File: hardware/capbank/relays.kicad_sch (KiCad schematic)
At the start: 13 parts, among them K1 3570.1333.121 COMUS, K2 3570.1333.121 COMUS, K4 3570.1333.121 COMUS, U1 ULN2003

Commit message: KiCad changes
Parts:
- added D10, D11, D9: LED, PCM_Diode_SMD_Handsoldering_AKL:D_0603_1608Metric, symbol Device:LED
- added R11, R12, R16: 1k, PCM_Resistor_SMD_AKL:R_0603_1608Metric, symbol Device:R
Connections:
- net GND: now also D10.1 (K), D11.1 (K), D9.1 (K)
- net RELAY_CTRL_1: now also R11.1
- net RELAY_CTRL_2: now also R12.1
- net RELAY_CTRL_3: now also R16.1
- new net: D10.2 (A), R12.2
- new net: D11.2 (A), R16.2
- new net: D9.2 (A), R11.2

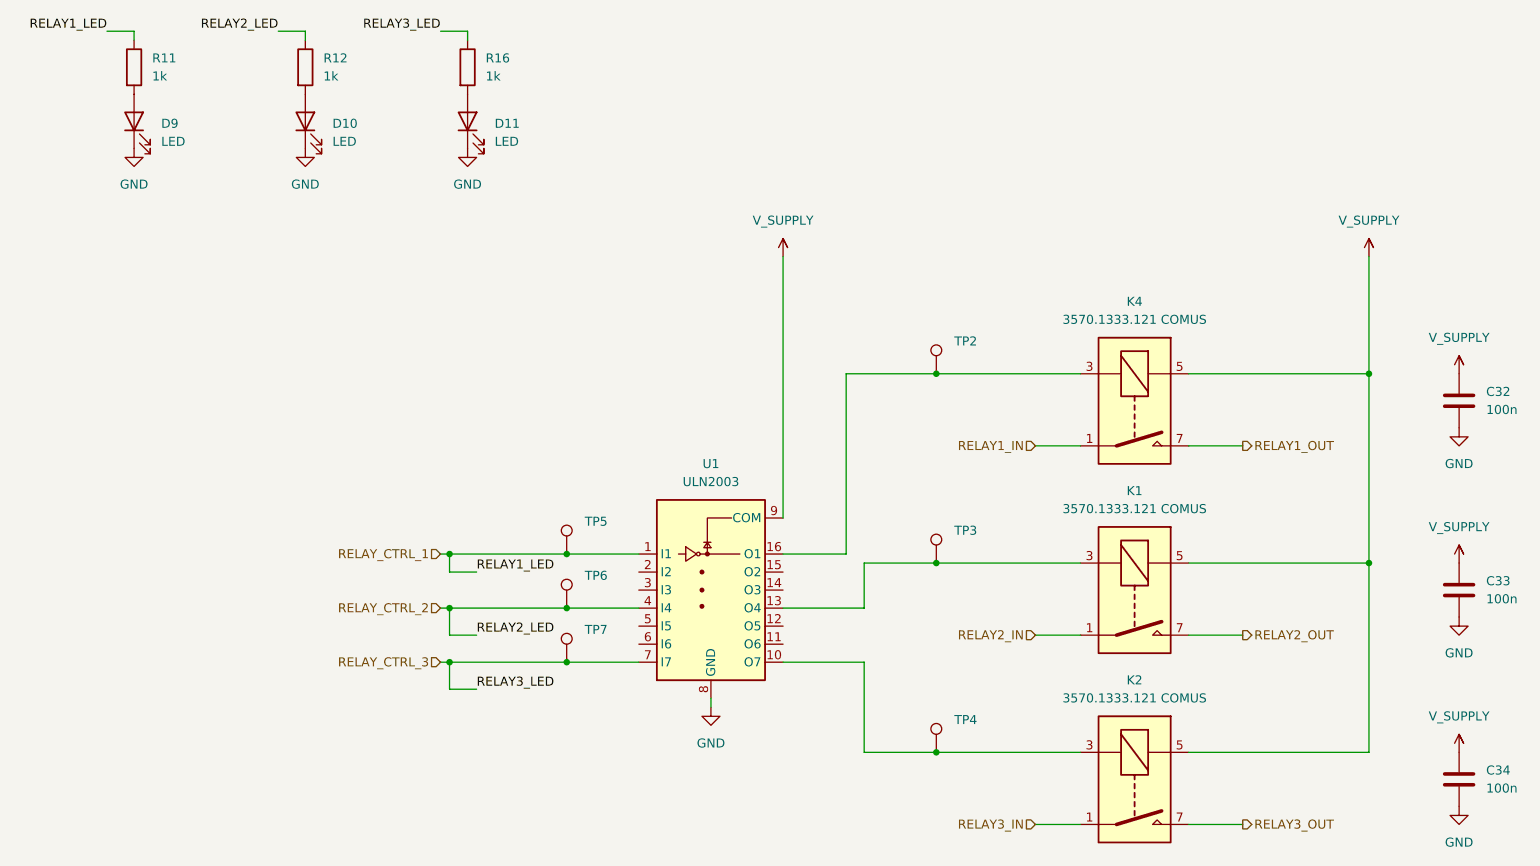
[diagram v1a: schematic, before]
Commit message: Progress, layout nearly completed, build oscillator on breadboard
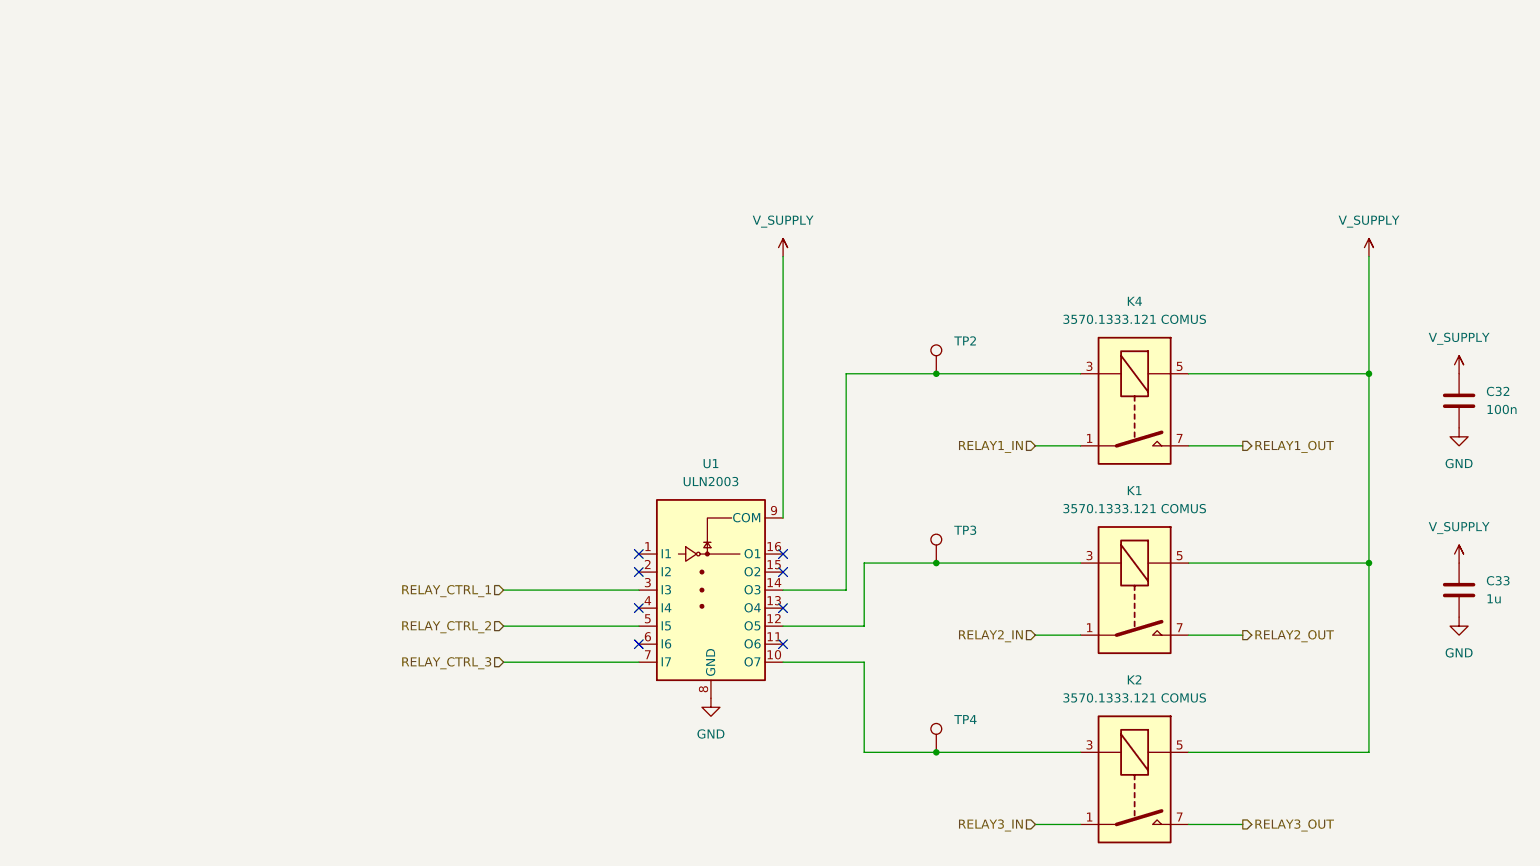
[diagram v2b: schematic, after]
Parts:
- removed C34: 100n, PCM_Capacitor_SMD_AKL:C_0603_1608Metric, symbol Device:C
- removed D10, D11, D9: LED, PCM_Diode_SMD_Handsoldering_AKL:D_0603_1608Metric, symbol Device:LED
- removed R11, R12, R16: 1k, PCM_Resistor_SMD_AKL:R_0603_1608Metric, symbol Device:R
- removed TP5, TP6, TP7: ~, TestPoint:TestPoint_THTPad_1.5x1.5mm_Drill0.7mm, symbol Connector:TestPoint
- C33: value 100n -> 1u
- U1: footprint Package_DIP:DIP-16_W7.62mm -> Package_SO:SOIC-16_3.9x9.9mm_P1.27mm
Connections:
- net RELAY_CTRL_1: now also U1.3 (I3); no longer U1.1 (I1)
- net RELAY_CTRL_2: now also U1.5 (I5); no longer U1.4 (I4)
- net at K4.3, TP2.1: now also U1.14 (O3); no longer U1.16 (O1)
- net at K1.3, TP3.1: now also U1.12 (O5); no longer U1.13 (O4)
- no-connect marks 0 -> 8
